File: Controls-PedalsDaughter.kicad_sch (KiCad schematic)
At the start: 22 parts, among them J1 PowerConn, J2 Accel Pos. Sensor, J3 PeripheralCANConnector, J4 Conn_01x02, U1 RI3-1205S, U2 PeripheralSOM, U4 TLV172IDCK, U5 NSL-32

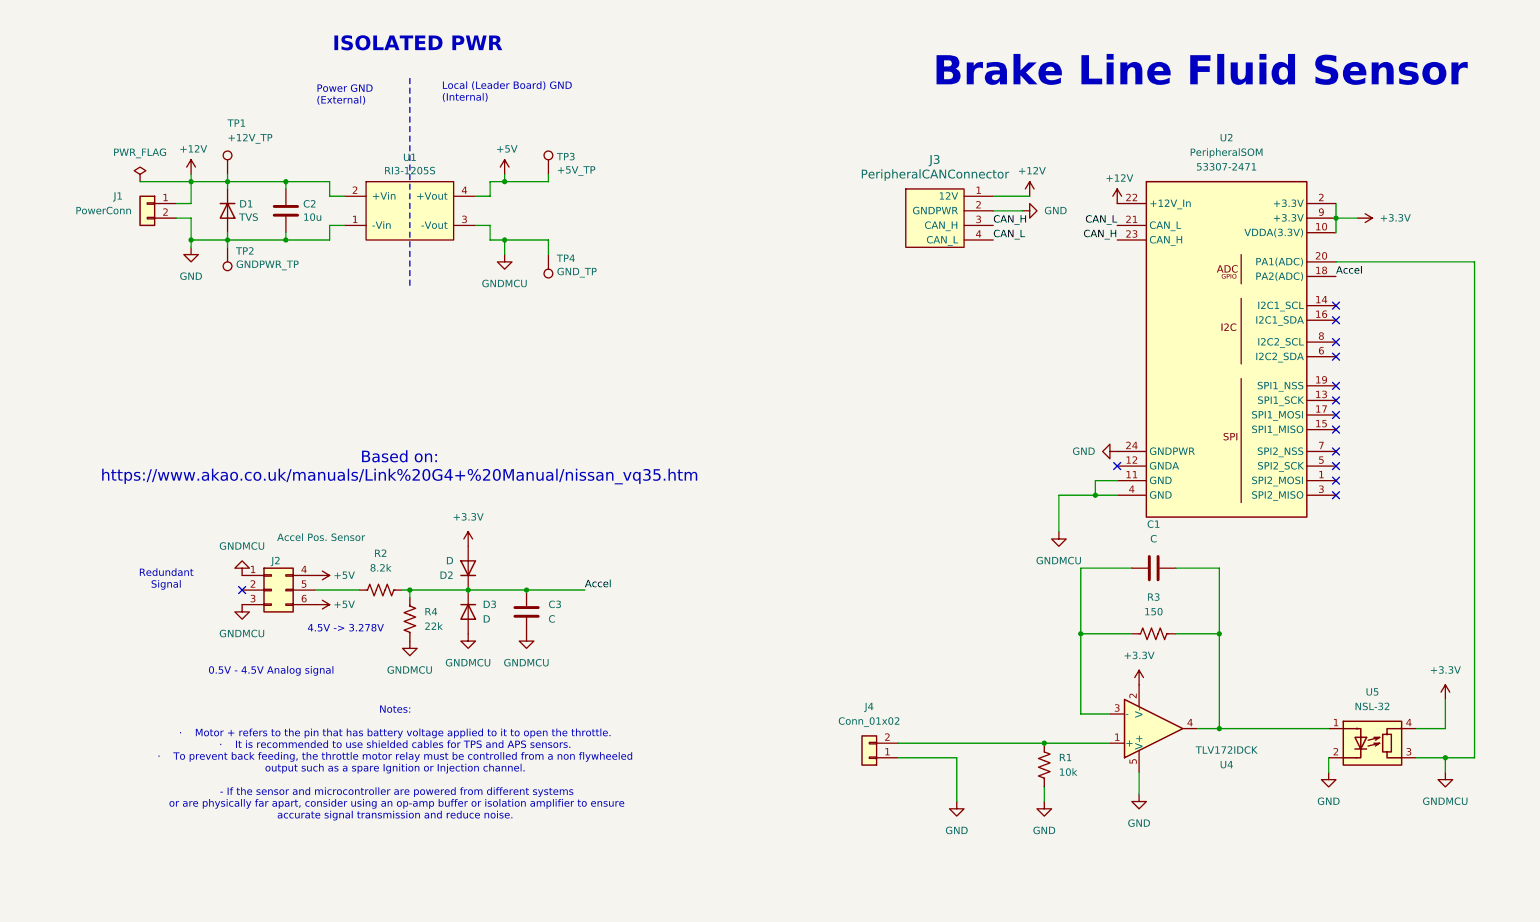
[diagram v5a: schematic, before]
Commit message: ERC Fixed
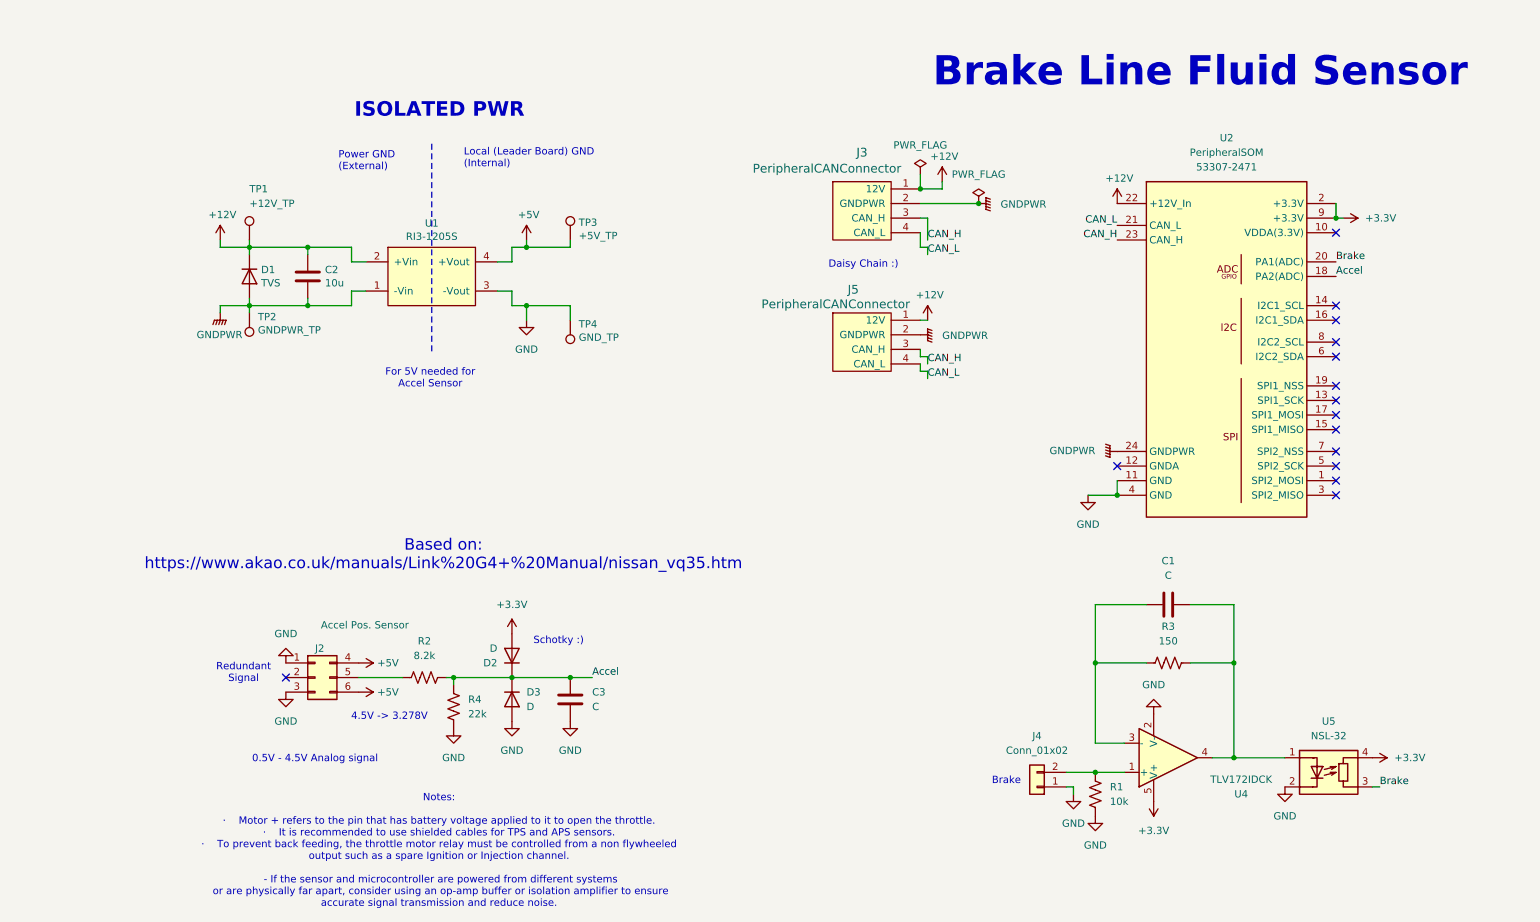
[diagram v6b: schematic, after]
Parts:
- removed J1: PowerConn, UTSVT_Connectors:Molex_MicroFit3.0_1x2xP3.00mm_PolarizingPeg_Vertical, symbol Connector_Generic:Conn_01x02
- added J5: PeripheralCANConnector, UTSVT_Connectors:Molex_MicroFit3.0_1x4xP3.00mm_PolarizingPeg_Vertical, symbol utsvt-connectors:PeripheralCANConnector
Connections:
- net +12V: now also J5.1 (12V)
- net +3.3V: now also U4.5 (V+); no longer U2.10 (VDDA(3.3V)), U4.2 (V-)
- net CAN_H: now also J5.3 (CAN_H)
- net CAN_L: now also J5.4 (CAN_L)
- net GND: now also C3.1, D3.2 (A), J2.1 (Pin_1), J2.3 (Pin_3), R4.2, TP4.1, U1.3 (-Vout), U2.11 (GND), U2.4 (GND), U4.2 (V-); no longer C2.2, D1.2 (A), J3.2 (GNDPWR), TP2.1, U1.1 (-Vin), U2.24 (GNDPWR), U4.5 (V+)
- removed net GNDMCU: C3.1, D3.2 (A), J2.1 (Pin_1), J2.3 (Pin_3), R4.2, TP4.1, U1.3 (-Vout), U2.11 (GND), U2.20 (PA1(ADC)), U2.4 (GND), U5.3 (R)
- new net Brake: U2.20 (PA1(ADC)), U5.3 (R)
- new net GNDPWR: C2.2, D1.2 (A), J3.2 (GNDPWR), J5.2 (GNDPWR), TP2.1, U1.1 (-Vin), U2.24 (GNDPWR)
- no-connect marks 14 -> 15
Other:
- note added: "Brake"
- note added: "Daisy Chain :)"
- note added: "For 5V needed for Accel Sensor"
- note added: "Schotky :)"
- moved on the sheet: C1, C2, C3, D1, D2, D3, J2, J3, J4, R1, R2, R3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

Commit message: Abt to change stuff
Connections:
- net +12V: now also U4.5 (V+)
- net +3.3V: no longer U4.5 (V+)
- net GND: no longer J4.1 (Pin_1), R1.2, U4.2 (V-)
- net GNDPWR: now also J4.1 (Pin_1), R1.2, U4.2 (V-)
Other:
- moved on the sheet: C1, J3, J4, J5, R1, R3, U2, U4, U5

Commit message: First Draft
✈️
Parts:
- removed R3: 150, symbol Device:R_US
- removed U4: TLV172IDCK, Package_TO_SOT_SMD:SOT-353_SC-70-5, symbol Amplifier_Operational:TLV172IDCK
- removed U5: NSL-32, OptoDevice:Luna_NSL-32, symbol Isolator:NSL-32
- added D4, D5: D, symbol Device:D
- C1: value C -> 1F
- R1: value 10k -> 160
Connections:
- net +3.3V: now also D2.1 (K), D4.1 (K); no longer D2.2 (A)
- net Accel: now also D2.2 (A); no longer D2.1 (K)
- net Brake: now also C1.1, J4.2 (Pin_2), R1.1, D4.2 (A), D5.1 (K)
- net GND: now also C1.2, J4.1 (Pin_1), R1.2, D5.2 (A)
- net GNDPWR: no longer J4.1 (Pin_1), R1.2
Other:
- note added: "Break Sensor to ADC"
- moved on the sheet: D2, J3, J4, J5, U2
